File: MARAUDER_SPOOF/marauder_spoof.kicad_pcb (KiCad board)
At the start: 2 copper layers, 67 x 28 mm, 44 parts, among them J1 Coil, J2 Conn_01x10_Socket, J3 Conn_01x08_Socket, J6 GPS, P1 USB_C_Plug_USB2.0, Q1 DMP2004TK-7, Q2 DMP2004TK-7, SW1 RESET, SW2 GPIO, U1 TC4424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

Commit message: Add_subg_BOM
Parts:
- Q1, Q2: footprint Package_TO_SOT_SMD:SOT-23 -> Package_TO_SOT_SMD:SOT-523
- moved Q1 1.69 mm to (224.1, 80.5), turned to 90 degrees
- moved Q2 0.83 mm to (224.0, 77.8), turned to 180 degrees
- moved R5 0.30 mm to (220.5, 77.7)
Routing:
- net Net-(Q1-G): track 7.10 -> 10.6 mm
- net Net-(Q1-D): track 7.73 -> 9.22 mm
- net Net-(Q1-S): track 2.04 -> 3.45 mm
- net Net-(Q2-S): track 2.05 -> 3.03 mm

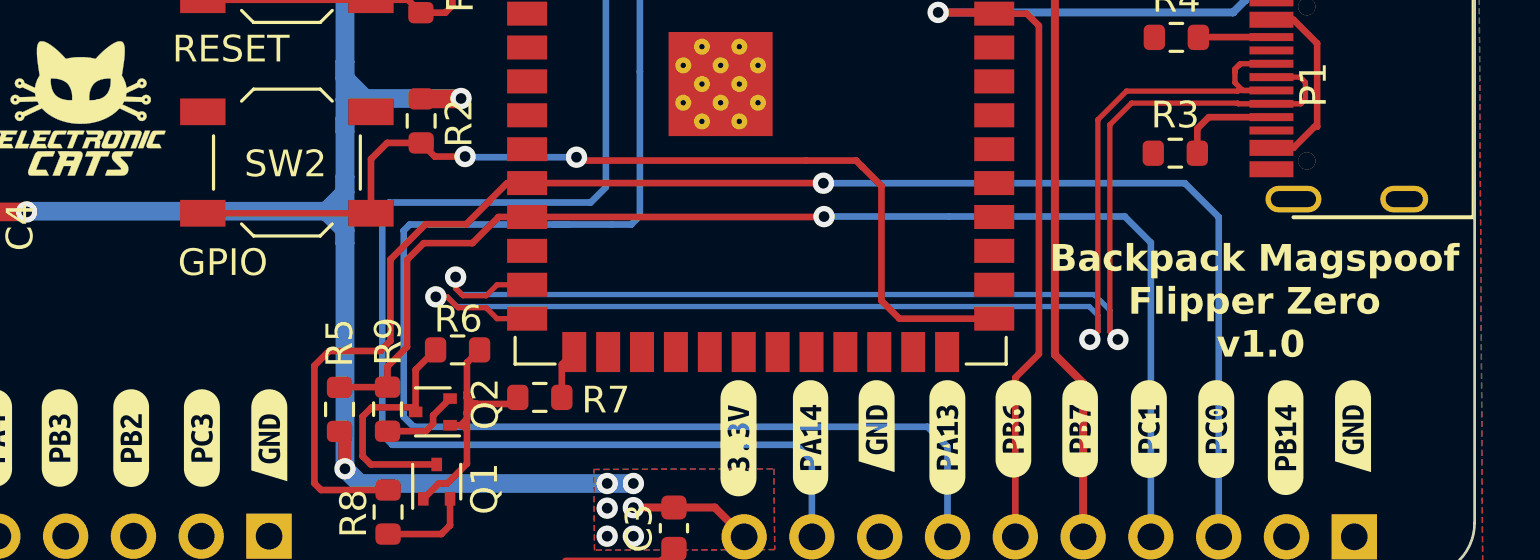
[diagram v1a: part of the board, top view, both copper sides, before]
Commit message: Board name and boot button label added in the marauder flipper
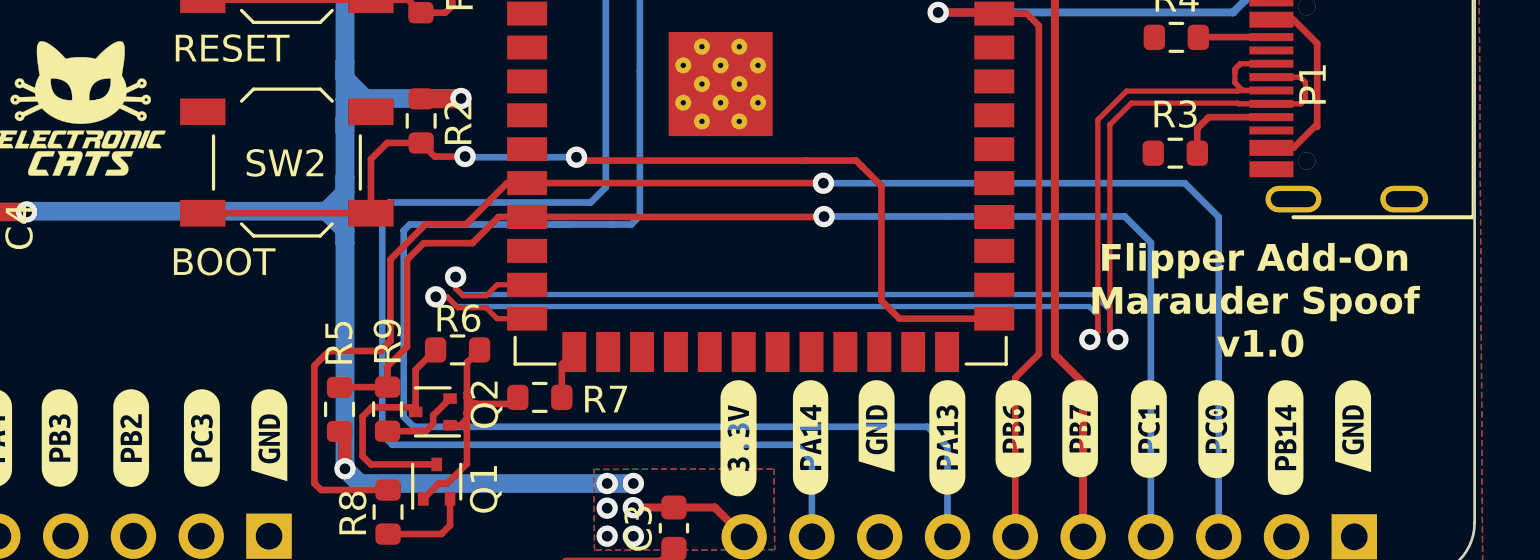
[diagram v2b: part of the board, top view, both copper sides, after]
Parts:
- SW2: value GPIO -> BOOT
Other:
- board text added: "Flipper Add-On Marauder Spoof v1.0"
- board text removed: "Backpack Magspoof Flipper Zero v1.0"
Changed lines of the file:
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@@
         (effects (font (size 1 1) (thickness 0.15)))
     )
-    (fp_text value "GPIO" (at -2.4 3.75) (layer "F.SilkS")
+    (fp_text value "BOOT" (at -2.4 3.75) (layer "F.SilkS")
         (effects (font (size 1 1) (thickness 0.15)))
     )
@@
   (gr_arc (start 261 56) (mid 262.414223 56.585781) (end 263 58)
     (stroke (width 0.1) (type default)) (layer "Edge.Cuts"))
-  (gr_text "Backpack Magspoof\nFlipper Zero\n v1.0" (at 254.75 73.7) (layer "F.SilkS")
+  (gr_text "Flipper Add-On\nMarauder Spoof\n v1.0" (at 254.75 73.7) (layer "F.SilkS")
     (effects (font (size 1 1) (thickness 0.25) bold))
   )

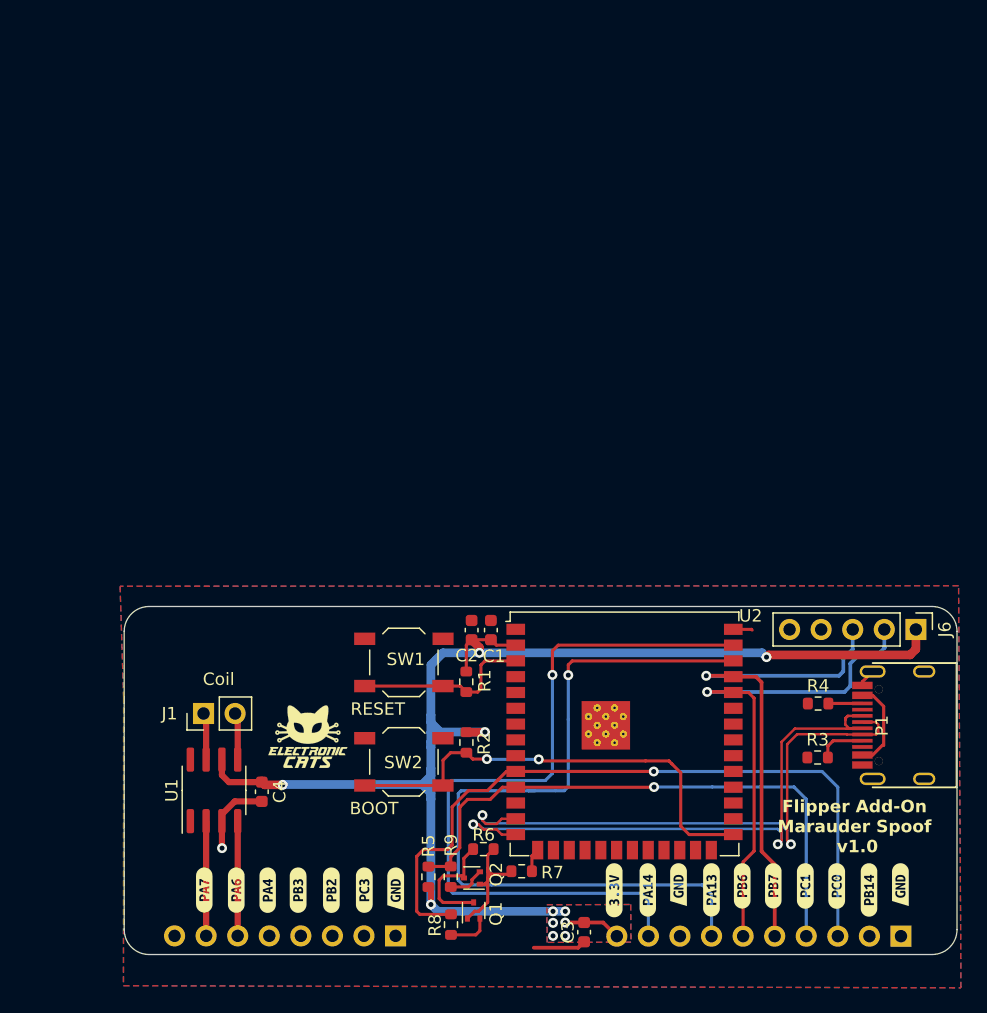
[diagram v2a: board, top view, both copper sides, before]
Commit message: feat(hw):Update coil
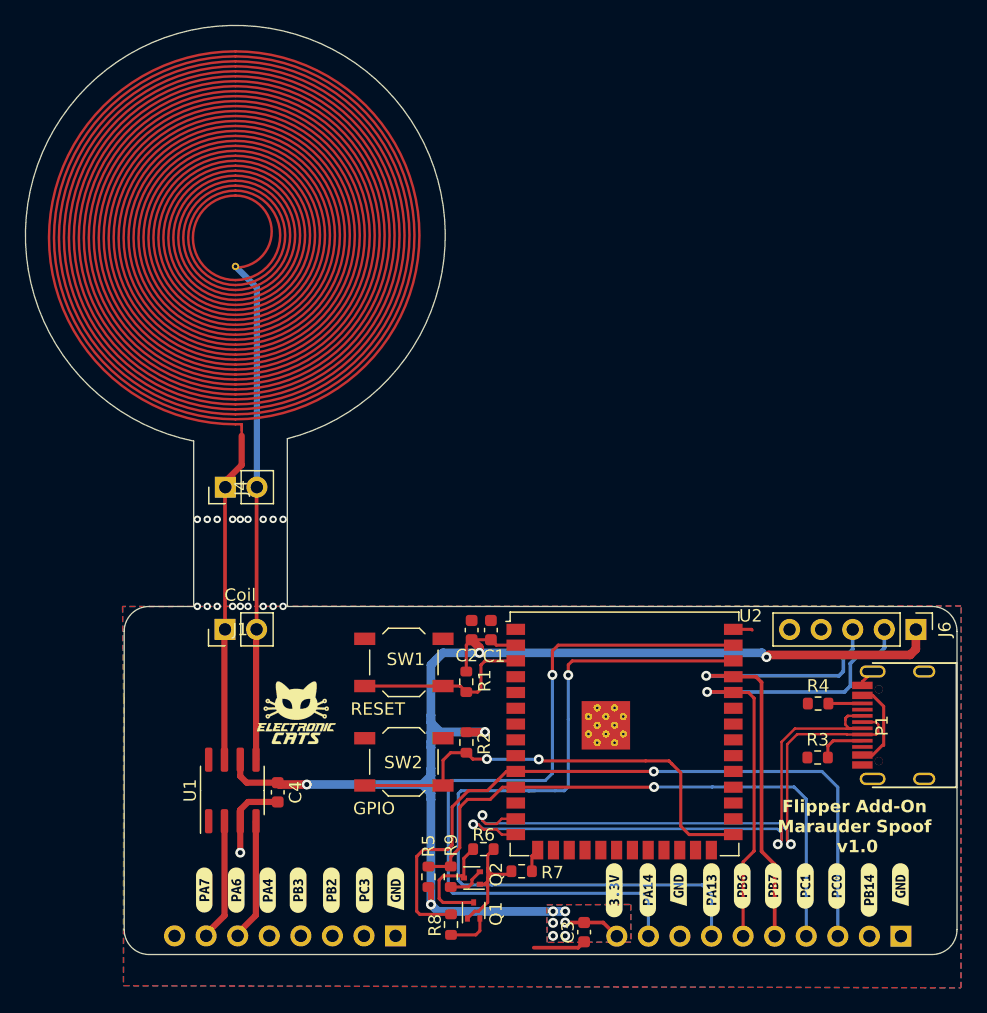
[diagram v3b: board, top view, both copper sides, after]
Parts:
- added J4: Coil, Connector_PinHeader_2.54mm:PinHeader_1x02_P2.54mm_Vertical, F.Cu at (204.1, 46.4)
- added L1: 30t_30mm, Library:Coil_30t_30mm_0.2_0.2_0.6_0.3, F.Cu at (204.9, 26.1)
- SW2: value BOOT -> GPIO
- U2: value ESP32-S3-WROOM-1U-N16 -> ESP32-S3-WROOM-1U-N4
- moved J1 6.99 mm to (204.1, 57.8)
- moved G*** 2.14 mm to (209.8, 64.5)
- moved U1 1.48 mm to (204.7, 70.8)
- moved C4 1.28 mm to (208.3, 71.0)
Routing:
- net /Out_B: track 3.80 -> 40.4 mm
- net /Out_A: track 3.80 -> 26.6 mm
- net unconnected-(P1-VBUS-PadA4)_0: track 7.24 -> 0.00 mm
- net unconnected-(P1-VBUS-PadA4): track 0.00 -> 7.24 mm
- net +3V3: track 116.4 -> 114.7 mm
- net /IN_A: track 9.23 -> 9.84 mm
- net /IN_B: track 9.24 -> 9.84 mm
- net GND: track 13.6 -> 14.0 mm, vias 1 -> 10
- net (no net): vias 0 -> 9
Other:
- board size 67 x 28 mm -> 74.9 x 74.7 mm

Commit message: fix(hw): add thickness comment
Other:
- board text added: "Flipper Add-On Marauder Spoof v1.1"
- board text added: "PCB tickness = 0.8 mm"
- board text removed: "Flipper Add-On Marauder Spoof v1.0"
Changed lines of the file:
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@@
 		)
 		(fp_text user "${REFERENCE}"
-			(at 0 1.27 360)
+			(at 0 1.27 0)
 			(layer "F.Fab")
 			(effects
@@
 		(layer "Edge.Cuts")
 	)
-	(gr_text "Flipper Add-On\nMarauder Spoof\n v1.0"
+	(gr_text "Flipper Add-On\nMarauder Spoof\n v1.1"
+		(at 254.92 73.75 -0)
+		(layer "B.SilkS")
+		(effects
+			(font
+				(size 1 1)
+				(thickness 0.25)
+				(bold yes)
+			)
+			(justify mirror)
+		)
+	)
+	(gr_text "Flipper Add-On\nMarauder Spoof\n v1.1"
 		(at 254.75 73.7 0)
 		(layer "F.SilkS")
@@
 		)
 	)
+	(gr_text "PCB tickness = 0.8 mm"
+		(at 196.9 88.84 0)
+		(layer "Cmts.User")
+		(effects
+			(font
+				(size 1 1)
+				(thickness 0.15)
+			)
+			(justify left bottom)
+		)
+	)
 	(dimension
 		(type aligned)
-		(layer "Margin")
+		(layer "Dwgs.User")
 		(pts
 			(xy 217.851 82.2032) (xy 200.071 82.2032)
@@
 		(gr_text "17.7800 mm"
 			(at 208.961 98.1 0)
-			(layer "Margin")
+			(layer "Dwgs.User")
 			(effects
 				(font
@@
 	(dimension
 		(type aligned)
-		(layer "Margin")
+		(layer "Dwgs.User")
 		(pts
 			(xy 200.8584 86.4602) (xy 200.8584 92.3946)
@@
 		(gr_text "5.9344 mm"
 			(at 176.8334 89.4274 90)
-			(layer "Margin")
+			(layer "Dwgs.User")
 			(effects
 				(font
@@
 	(dimension
 		(type aligned)
-		(layer "Margin")
+		(layer "Dwgs.User")
 		(pts
 			(xy 235.551 82.8232) (xy 217.771 82.8232)
@@
 		(gr_text "17.7800 mm"
 			(at 226.661 95.49 0)
-			(layer "Margin")
+			(layer "Dwgs.User")
 			(effects
 				(font
@@
 	(dimension
 		(type aligned)
-		(layer "Margin")
+		(layer "Dwgs.User")
 		(pts
 			(xy 258.491 82.2032) (xy 235.631 82.2032)
@@
 		(gr_text "22.8600 mm"
 			(at 247.061 97.26 0)
-			(layer "Margin")
+			(layer "Dwgs.User")
 			(effects
 				(font

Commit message: feat: rename addons
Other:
- board text added: "Flipper Addon Marauder Spoof v1.1"
- board text removed: "Flipper Add-On Marauder Spoof v1.1"
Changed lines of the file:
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@@
 		(layer "Edge.Cuts")
 	)
-	(gr_text "Flipper Add-On\nMarauder Spoof\n v1.1"
-		(at 254.92 73.75 -0)
+	(gr_text "Flipper Addon\nMarauder Spoof\n v1.1"
+		(at 254.92 73.75 0)
 		(layer "B.SilkS")
 		(effects
@@
 		)
 	)
-	(gr_text "Flipper Add-On\nMarauder Spoof\n v1.1"
+	(gr_text "Flipper Addon\nMarauder Spoof\n v1.1"
 		(at 254.75 73.7 0)
 		(layer "F.SilkS")

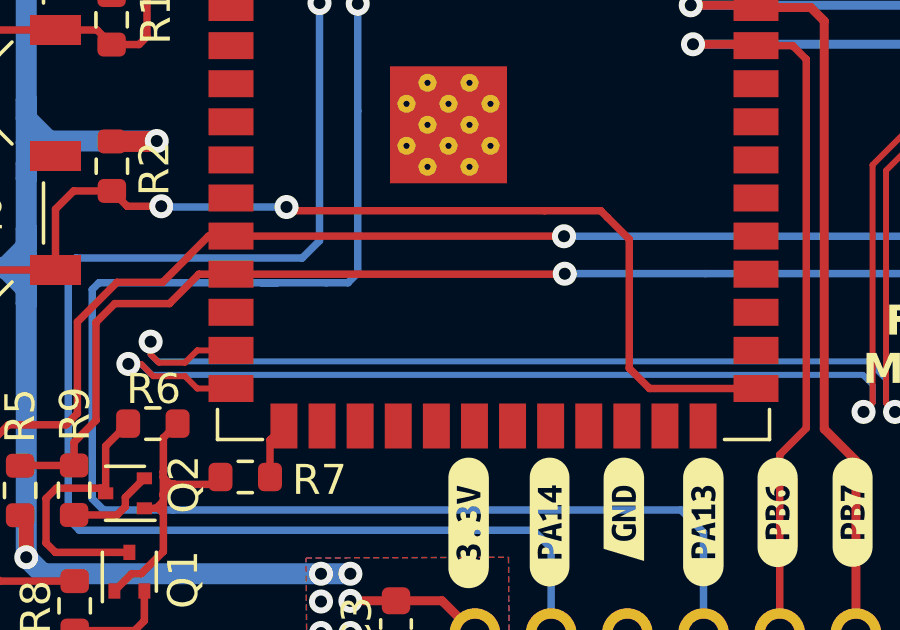
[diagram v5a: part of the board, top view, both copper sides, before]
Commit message: fix(hw): add gnd vias
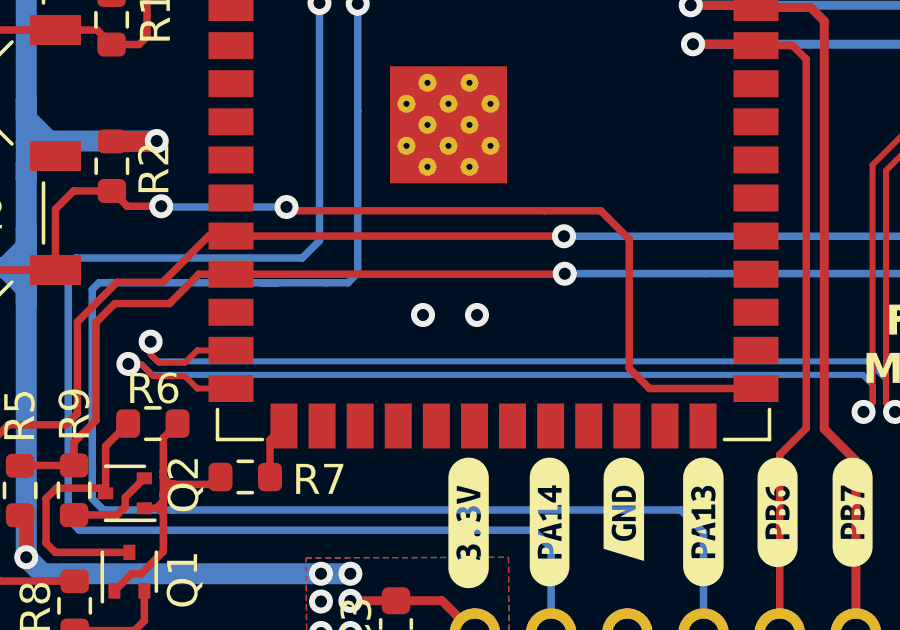
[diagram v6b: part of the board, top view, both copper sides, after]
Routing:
- net GND: vias 10 -> 12

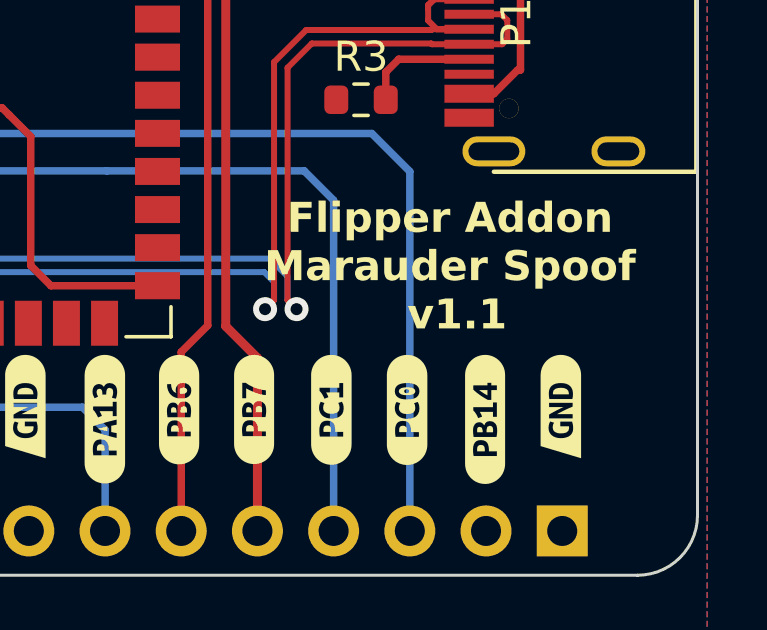
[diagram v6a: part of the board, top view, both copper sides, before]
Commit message: feat(hw): Update Marauder-Spoof version label
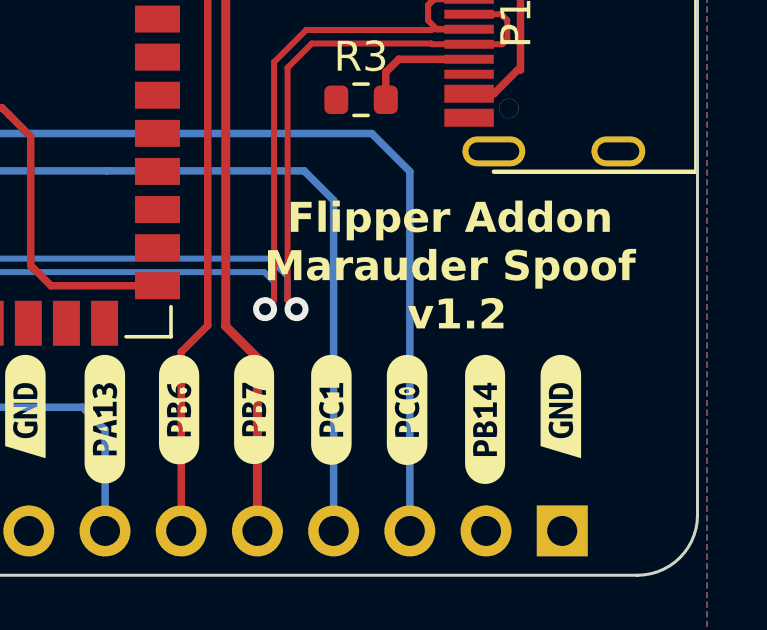
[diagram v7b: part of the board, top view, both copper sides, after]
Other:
- board text added: "Flipper Addon Marauder Spoof v1.2"
- board text removed: "Flipper Addon Marauder Spoof v1.1"
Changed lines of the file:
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@@
 		(layer "Edge.Cuts")
 	)
-	(gr_text "Flipper Addon\nMarauder Spoof\n v1.1"
+	(gr_text "Flipper Addon\nMarauder Spoof\n v1.2"
 		(at 254.75 73.7 0)
 		(layer "F.SilkS")
@@
 		)
 	)
-	(gr_text "Flipper Addon\nMarauder Spoof\n v1.1"
+	(gr_text "Flipper Addon\nMarauder Spoof\n v1.2"
 		(at 254.92 73.75 0)
 		(layer "B.SilkS")
